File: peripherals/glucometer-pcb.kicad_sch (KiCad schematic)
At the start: 10 parts, among them U1 ESP32_DevKit_V1_DOIT

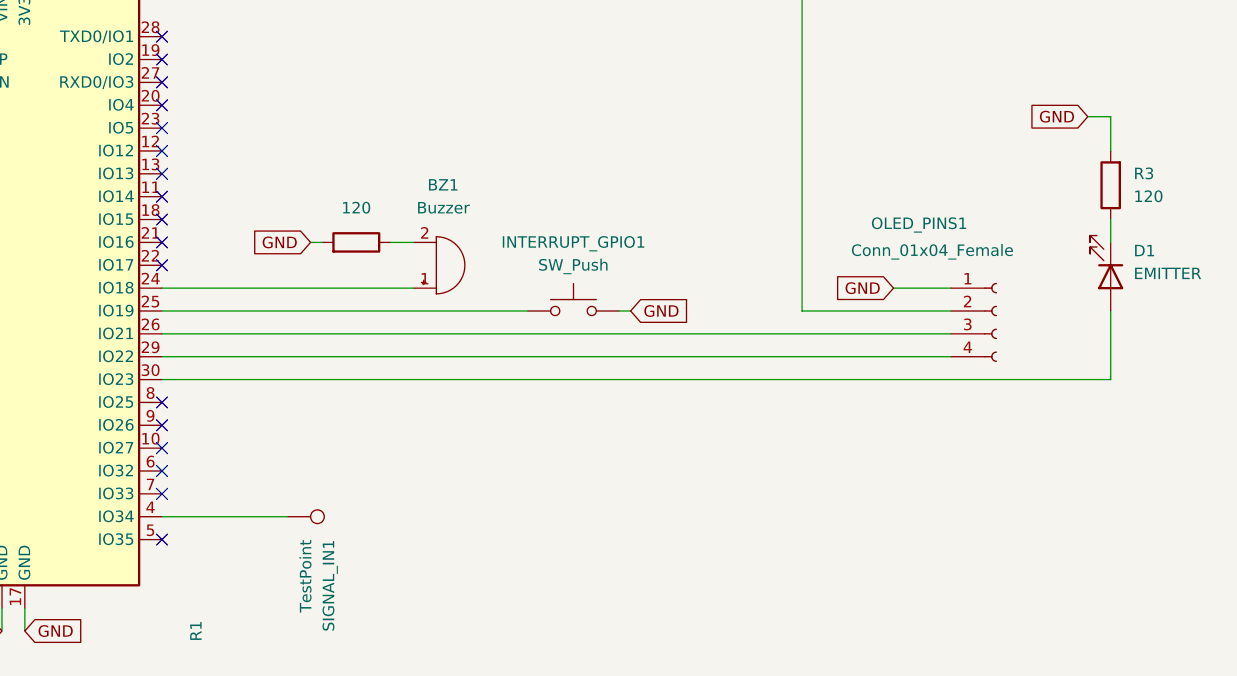
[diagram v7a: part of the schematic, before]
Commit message: updated footprints
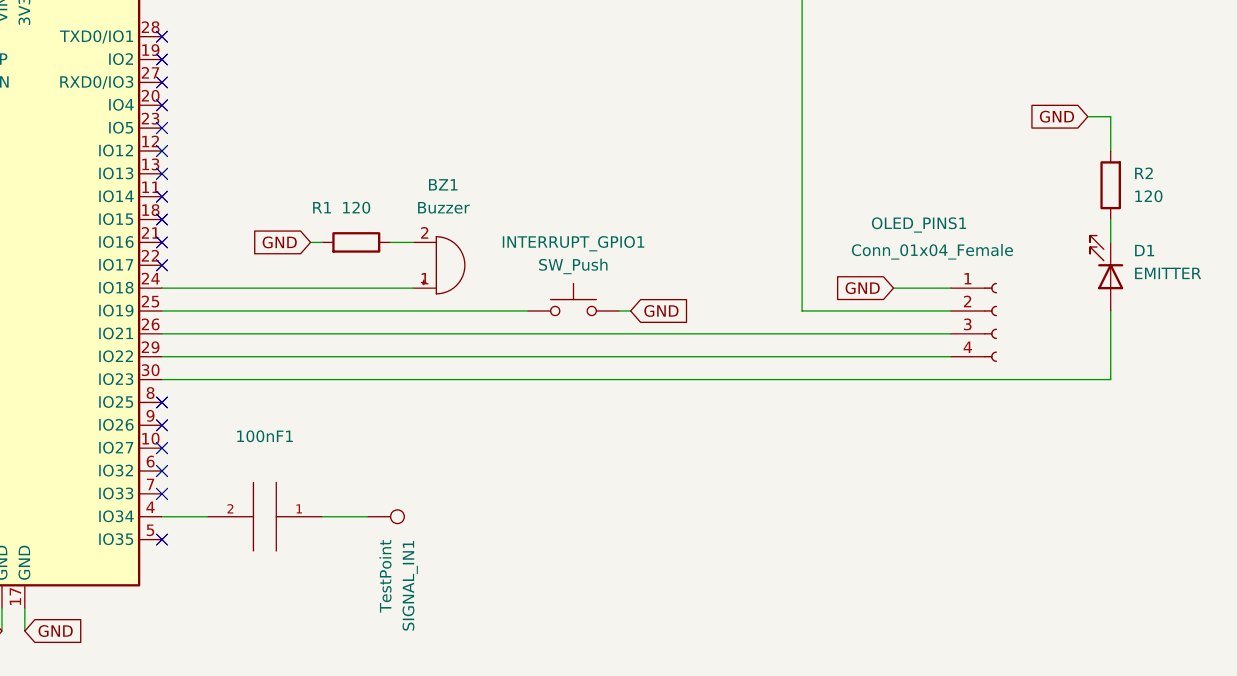
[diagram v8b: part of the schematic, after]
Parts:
- added 100nF1: (no value), symbol pspice:CAP
- BZ1: footprint Buzzer_Beeper:MagneticBuzzer_Kingstate_KCG0601 -> (none)
- renumbered R3 to R2
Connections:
- net at SIGNAL_IN1.1: now also 100nF1.1; no longer U1.4 (IO34)
- new net: 100nF1.2, U1.4 (IO34)
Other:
- moved on the sheet: SIGNAL_IN1
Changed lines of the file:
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@@
+    (stroke (width 0) (type default) (color 0 0 0 0))
+  )
+  (wire (pts (xy 101.6 116.84) (xy 106.68 116.84))
     (stroke (width 0) (type default) (color 0 0 0 0))
   )
@@
     (stroke (width 0) (type default) (color 0 0 0 0))
   )
+  (wire (pts (xy 83.82 116.84) (xy 88.9 116.84))
+    (stroke (width 0) (type default) (color 0 0 0 0))
+  )
   (wire (pts (xy 189.23 83.82) (xy 189.23 86.36))
     (stroke (width 0) (type default) (color 0 0 0 0))
@@
   )
   (wire (pts (xy 68.58 48.26) (xy 68.58 55.88))
-    (stroke (width 0) (type default) (color 0 0 0 0))
-  )
-  (wire (pts (xy 83.82 116.84) (xy 97.79 116.84))
     (stroke (width 0) (type default) (color 0 0 0 0))
   )
@@
   (symbol (lib_id "Device:R") (at 105.41 86.36 270) (mirror x) (unit 1)
     (in_bom yes) (on_board yes)
-    (property "Reference" "R1" (id 0) (at 87.63 129.54 0))
+    (property "Reference" "R1" (id 0) (at 101.6 82.55 90))
     (property "Value" "120" (id 1) (at 105.41 82.55 90))
     (property "Footprint" "Resistor_THT:R_Axial_DIN0204_L3.6mm_D1.6mm_P7.62mm_Horizontal" (id 2) (at 105.41 88.138 90)
@@
     (pin "1")
   )
+  (symbol (lib_id "pspice:CAP") (at 95.25 116.84 270) (unit 1)
+    (in_bom yes) (on_board yes) (fields_autoplaced)
+    (property "Reference" "100nF1" (id 0) (at 95.25 107.95 90))
+    (property "Value" "" (id 1) (at 95.25 110.49 90))
+    (property "Footprint" "" (id 2) (at 95.25 116.84 0)
+      (effects (font (size 1.27 1.27)) hide)
+    )
+    (property "Datasheet" "~" (id 3) (at 95.25 116.84 0)
+      (effects (font (size 1.27 1.27)) hide)
+    )
+    (pin "1")
+    (pin "2")
+  )
   (symbol (lib_id "Device:LED") (at 189.23 90.17 270) (unit 1)
     (in_bom yes) (on_board yes) (fields_autoplaced)
@@
   (symbol (lib_id "Device:R") (at 189.23 80.01 180) (unit 1)
     (in_bom yes) (on_board yes) (fields_autoplaced)
-    (property "Reference" "R3" (id 0) (at 191.77 78.7399 0)
+    (property "Reference" "R2" (id 0) (at 191.77 78.7399 0)
       (effects (font (size 1.27 1.27)) (justify right))
     )
@@
     (property "Reference" "BZ1" (id 0) (at 115.062 80.01 0))
     (property "Value" "Buzzer" (id 1) (at 115.062 82.55 0))
-    (property "Footprint" "Buzzer_Beeper:MagneticBuzzer_Kingstate_KCG0601" (id 2) (at 113.665 91.44 90)
+    (property "Footprint" "" (id 2) (at 113.665 91.44 90)
       (effects (font (size 1.27 1.27)) hide)
     )
@@
     (pin "2")
   )
-  (symbol (lib_id "Connector:TestPoint") (at 97.79 116.84 270) (mirror x) (unit 1)
-    (in_bom yes) (on_board yes) (fields_autoplaced)
-    (property "Reference" "SIGNAL_IN1" (id 0) (at 102.3621 119.38 0)
+  (symbol (lib_id "Connector:TestPoint") (at 106.68 116.84 270) (mirror x) (unit 1)
+    (in_bom yes) (on_board yes) (fields_autoplaced)
+    (property "Reference" "SIGNAL_IN1" (id 0) (at 111.2521 119.38 0)
       (effects (font (size 1.27 1.27)) (justify right))
     )
-    (property "Value" "TestPoint" (id 1) (at 99.8221 119.38 0)
+    (property "Value" "TestPoint" (id 1) (at 108.7121 119.38 0)
       (effects (font (size 1.27 1.27)) (justify right))
     )
-    (property "Footprint" "TestPoint:TestPoint_Keystone_5015_Micro-Minature" (id 2) (at 97.79 111.76 0)
-      (effects (font (size 1.27 1.27)) hide)
-    )
-    (property "Datasheet" "~" (id 3) (at 97.79 111.76 0)
+    (property "Footprint" "TestPoint:TestPoint_Keystone_5015_Micro-Minature" (id 2) (at 106.68 111.76 0)
+      (effects (font (size 1.27 1.27)) hide)
+    )
+    (property "Datasheet" "~" (id 3) (at 106.68 111.76 0)
       (effects (font (size 1.27 1.27)) hide)
     )
@@
       (reference "3V3_OUT1") (unit 1) (value "TestPoint") (footprint "TestPoint:TestPoint_Keystone_5015_Micro-Minature")
     )
+    (path "/294ee031-8eaf-4cf8-90b3-ca0c458cba56"
+      (reference "100nF1") (unit 1) (value "CAP") (footprint "Capacitor_THT:C_Disc_D4.3mm_W1.9mm_P5.00mm")
+    )
     (path "/5e026086-a6bc-405e-aa2b-27112efb7a35"
       (reference "BATTERY1") (unit 1) (value "Battery_Cell") (footprint "Connector_Wire:SolderWire-0.1sqmm_1x02_P3.6mm_D0.4mm_OD1mm")
     )
     (path "/5e4caf29-9a12-4f75-a8fa-7da0ee273177"
-      (reference "BZ1") (unit 1) (value "Buzzer") (footprint "Buzzer_Beeper:MagneticBuzzer_Kingstate_KCG0601")
+      (reference "BZ1") (unit 1) (value "Buzzer") (footprint "Buzzer_Beeper:MagneticBuzzer_ProSignal_ABI-009-RC")
     )
     (path "/44e0bd61-4827-43de-b1b9-a386bb6336c2"
@@
     )
     (path "/48716155-f70c-423a-8030-4a2d322cc6d9"
-      (reference "R3") (unit 1) (value "120") (footprint "Resistor_THT:R_Axial_DIN0204_L3.6mm_D1.6mm_P7.62mm_Horizontal")
+      (reference "R2") (unit 1) (value "120") (footprint "Resistor_THT:R_Axial_DIN0204_L3.6mm_D1.6mm_P7.62mm_Horizontal")
     )
     (path "/61259d1a-256c-4970-9afa-3c8c42ac6410"
